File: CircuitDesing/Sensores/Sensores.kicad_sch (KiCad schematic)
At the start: 6 parts

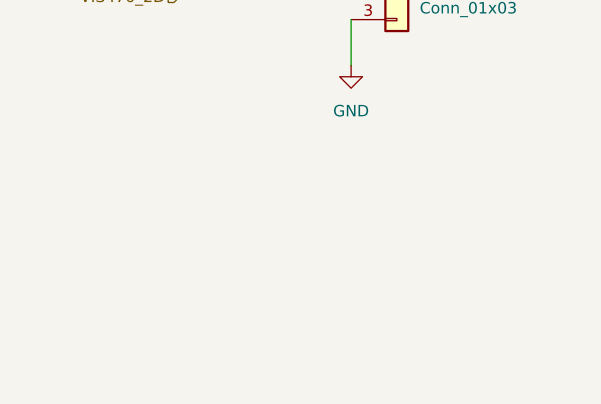
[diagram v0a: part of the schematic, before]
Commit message: Conector REED SWITCH PARA PUERTA
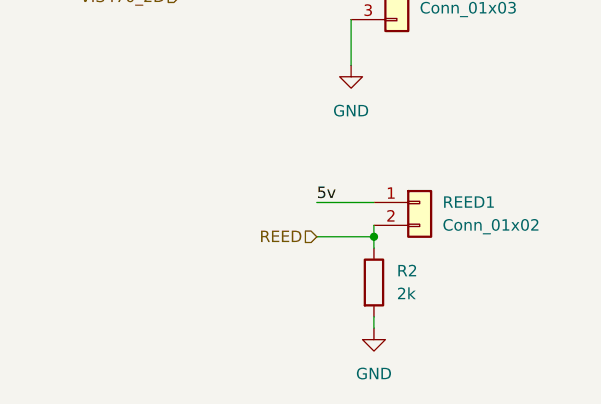
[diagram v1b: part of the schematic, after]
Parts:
- added R2: 2k, Resistor_SMD:R_0603_1608Metric_Pad0.98x0.95mm_HandSolder, symbol Device:R
- added REED1: Conn_01x02, symbol Connector_Generic:Conn_01x02
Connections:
- net 5v: now also REED1.1 (Pin_1)
- net GND: now also R2.2
- new net REED: R2.1, REED1.2 (Pin_2)
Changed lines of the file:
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@@
 (kicad_sch (version 20211123) (generator eeschema)
   (paper "A4")
+  (junction (at 139.7 154.94) (diameter 0) (color 0 0 0 0)
+  )
   (wire (pts (xy 139.7 66.04) (xy 139.7 76.2))
     (stroke (width 0) (type default) (color 0 0 0 0))
@@
     (stroke (width 0) (type default) (color 0 0 0 0))
   )
+  (wire (pts (xy 133.35 151.13) (xy 139.7 151.13))
+    (stroke (width 0) (type default) (color 0 0 0 0))
+  )
   (wire (pts (xy 142.24 66.04) (xy 139.7 66.04))
     (stroke (width 0) (type default) (color 0 0 0 0))
@@
     (stroke (width 0) (type default) (color 0 0 0 0))
   )
+  (wire (pts (xy 139.7 153.67) (xy 139.7 154.94))
+    (stroke (width 0) (type default) (color 0 0 0 0))
+  )
   (wire (pts (xy 50.8 97.79) (xy 69.85 97.79))
     (stroke (width 0) (type default) (color 0 0 0 0))
@@
     (stroke (width 0) (type default) (color 0 0 0 0))
   )
+  (wire (pts (xy 139.7 163.83) (xy 139.7 165.1))
+    (stroke (width 0) (type default) (color 0 0 0 0))
+  )
   (wire (pts (xy 68.58 119.38) (xy 68.58 124.46))
     (stroke (width 0) (type default) (color 0 0 0 0))
@@
     (stroke (width 0) (type default) (color 0 0 0 0))
   )
+  (wire (pts (xy 133.35 154.94) (xy 139.7 154.94))
+    (stroke (width 0) (type default) (color 0 0 0 0))
+  )
   (wire (pts (xy 69.85 100.33) (xy 69.85 105.41))
     (stroke (width 0) (type default) (color 0 0 0 0))
@@
     (stroke (width 0) (type default) (color 0 0 0 0))
   )
+  (wire (pts (xy 139.7 154.94) (xy 139.7 156.21))
+    (stroke (width 0) (type default) (color 0 0 0 0))
+  )
   (text "Sensor de humedad de aire y temperatura" (at 40.64 91.44 0)
     (effects (font (size 1.27 1.27)) (justify left bottom))
@@
     (effects (font (size 1.27 1.27)) (justify left bottom))
   )
+  (label "5v" (at 133.35 151.13 0)
+    (effects (font (size 1.27 1.27)) (justify left bottom))
+  )
   (hierarchical_label "DHT11_1D" (shape input) (at 50.8 64.77 180)
     (effects (font (size 1.27 1.27)) (justify right))
@@
   )
   (hierarchical_label "5v" (shape input) (at 45.72 40.64 180)
+    (effects (font (size 1.27 1.27)) (justify right))
+  )
+  (hierarchical_label "REED" (shape input) (at 133.35 154.94 180)
     (effects (font (size 1.27 1.27)) (justify right))
   )
@@
     (pin "3")
   )
+  (symbol (lib_id "power:GND") (at 139.7 165.1 0) (unit 1)
+    (in_bom yes) (on_board yes) (fields_autoplaced)
+    (property "Reference" "#PWR?" (id 0) (at 139.7 171.45 0)
+      (effects (font (size 1.27 1.27)) hide)
+    )
+    (property "Value" "GND" (id 1) (at 139.7 170.18 0))
+    (property "Footprint" "" (id 2) (at 139.7 165.1 0)
+      (effects (font (size 1.27 1.27)) hide)
+    )
+    (property "Datasheet" "" (id 3) (at 139.7 165.1 0)
+      (effects (font (size 1.27 1.27)) hide)
+    )
+    (pin "1")
+  )
   (symbol (lib_id "power:GND") (at 68.58 134.62 0) (unit 1)
     (in_bom yes) (on_board yes) (fields_autoplaced)
@@
     (pin "1")
   )
+  (symbol (lib_id "Connector_Generic:Conn_01x02") (at 144.78 151.13 0) (unit 1)
+    (in_bom yes) (on_board yes) (fields_autoplaced)
+    (property "Reference" "REED1" (id 0) (at 147.32 151.1299 0)
+      (effects (font (size 1.27 1.27)) (justify left))
+    )
+    (property "Value" "Conn_01x02" (id 1) (at 147.32 153.6699 0)
+      (effects (font (size 1.27 1.27)) (justify left))
+    )
+    (property "Footprint" "" (id 2) (at 144.78 151.13 0)
+      (effects (font (size 1.27 1.27)) hide)
+    )
+    (property "Datasheet" "~" (id 3) (at 144.78 151.13 0)
+      (effects (font (size 1.27 1.27)) hide)
+    )
+    (pin "1")
+    (pin "2")
+  )
+  (symbol (lib_id "Device:R") (at 139.7 160.02 0) (unit 1)
+    (in_bom yes) (on_board yes) (fields_autoplaced)
+    (property "Reference" "R2" (id 0) (at 142.24 158.7499 0)
+      (effects (font (size 1.27 1.27)) (justify left))
+    )
+    (property "Value" "2k" (id 1) (at 142.24 161.2899 0)
+      (effects (font (size 1.27 1.27)) (justify left))
+    )
+    (property "Footprint" "Resistor_SMD:R_0603_1608Metric_Pad0.98x0.95mm_HandSolder" (id 2) (at 137.922 160.02 90)
+      (effects (font (size 1.27 1.27)) hide)
+    )
+    (property "Datasheet" "~" (id 3) (at 139.7 160.02 0)
+      (effects (font (size 1.27 1.27)) hide)
+    )
+    (pin "1")
+    (pin "2")
+  )
   (symbol (lib_id "Connector_Generic:Conn_01x04") (at 147.32 66.04 0) (unit 1)

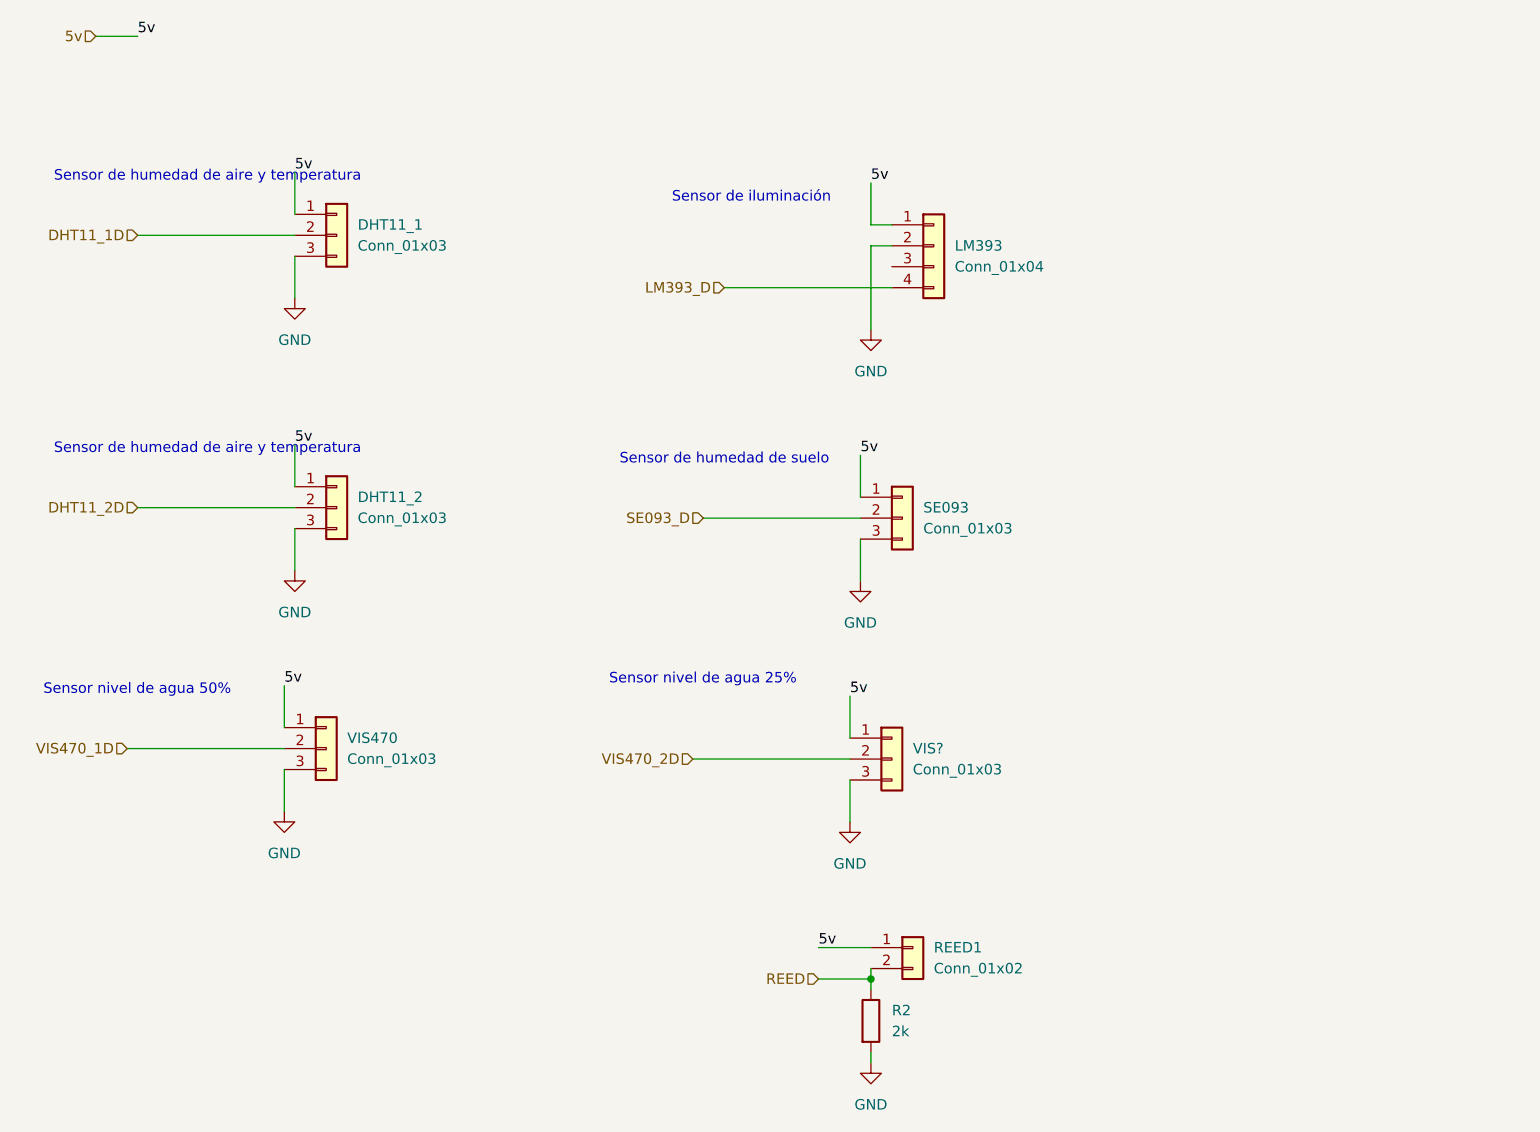
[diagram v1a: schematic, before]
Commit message: Actualizaciones de pines (Ultrasonido)
Cambios en la ubicación de pines para conexión con otros grupos.
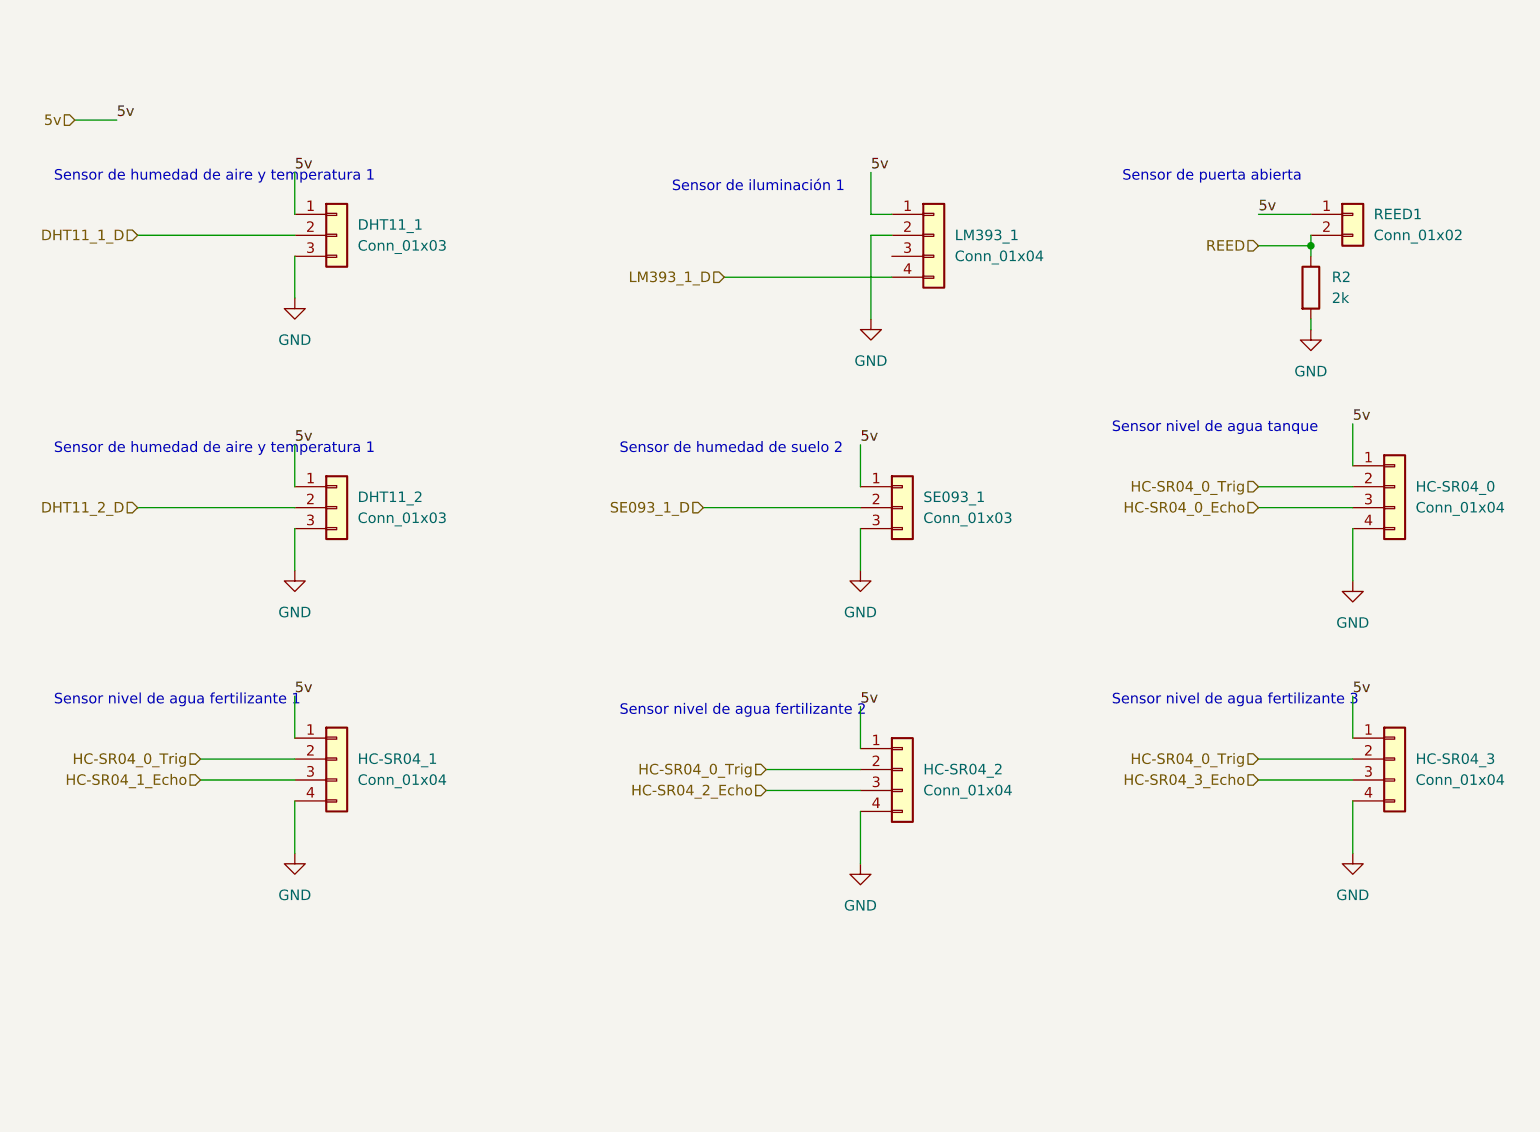
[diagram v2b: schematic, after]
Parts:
- removed VIS470, VIS?: Conn_01x03, symbol Connector_Generic:Conn_01x03
- added HC-SR04_0, HC-SR04_1, HC-SR04_2, HC-SR04_3: Conn_01x04, symbol Connector_Generic:Conn_01x04
- renumbered LM393 to LM393_1, SE093 to SE093_1
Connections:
- net 5v: now also HC-SR04_0.1 (Pin_1), HC-SR04_1.1 (Pin_1), HC-SR04_2.1 (Pin_1), HC-SR04_3.1 (Pin_1)
- net GND: now also HC-SR04_0.4 (Pin_4), HC-SR04_1.4 (Pin_4), HC-SR04_2.4 (Pin_4), HC-SR04_3.4 (Pin_4)
- net DHT11_1D renamed DHT11_1_D
- net DHT11_2D renamed DHT11_2_D
- net LM393_D renamed LM393_1_D
- net SE093_D renamed SE093_1_D
- new net HC-SR04_0_Echo: HC-SR04_0.3 (Pin_3)
- new net HC-SR04_0_Trig: HC-SR04_0.2 (Pin_2), HC-SR04_1.2 (Pin_2), HC-SR04_2.2 (Pin_2), HC-SR04_3.2 (Pin_2)
- new net HC-SR04_1_Echo: HC-SR04_1.3 (Pin_3)
- new net HC-SR04_2_Echo: HC-SR04_2.3 (Pin_3)
- new net HC-SR04_3_Echo: HC-SR04_3.3 (Pin_3)
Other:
- note added: "Sensor de humedad de aire y temperatura 1"
- note added: "Sensor de humedad de suelo 2"
- note added: "Sensor de iluminación 1"
- note added: "Sensor de puerta abierta"
- note added: "Sensor nivel de agua fertilizante 1"
- note added: "Sensor nivel de agua fertilizante 2"
- note added: "Sensor nivel de agua fertilizante 3"
- note added: "Sensor nivel de agua tanque"
- note removed: "Sensor de humedad de aire y temperatura"
- note removed: "Sensor de humedad de suelo"
- note removed: "Sensor de iluminación"
- note removed: "Sensor nivel de agua 25%"
- note removed: "Sensor nivel de agua 50%"
- moved on the sheet: LM393_1, R2, REED1, SE093_1
